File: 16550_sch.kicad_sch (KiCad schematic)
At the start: 1 part

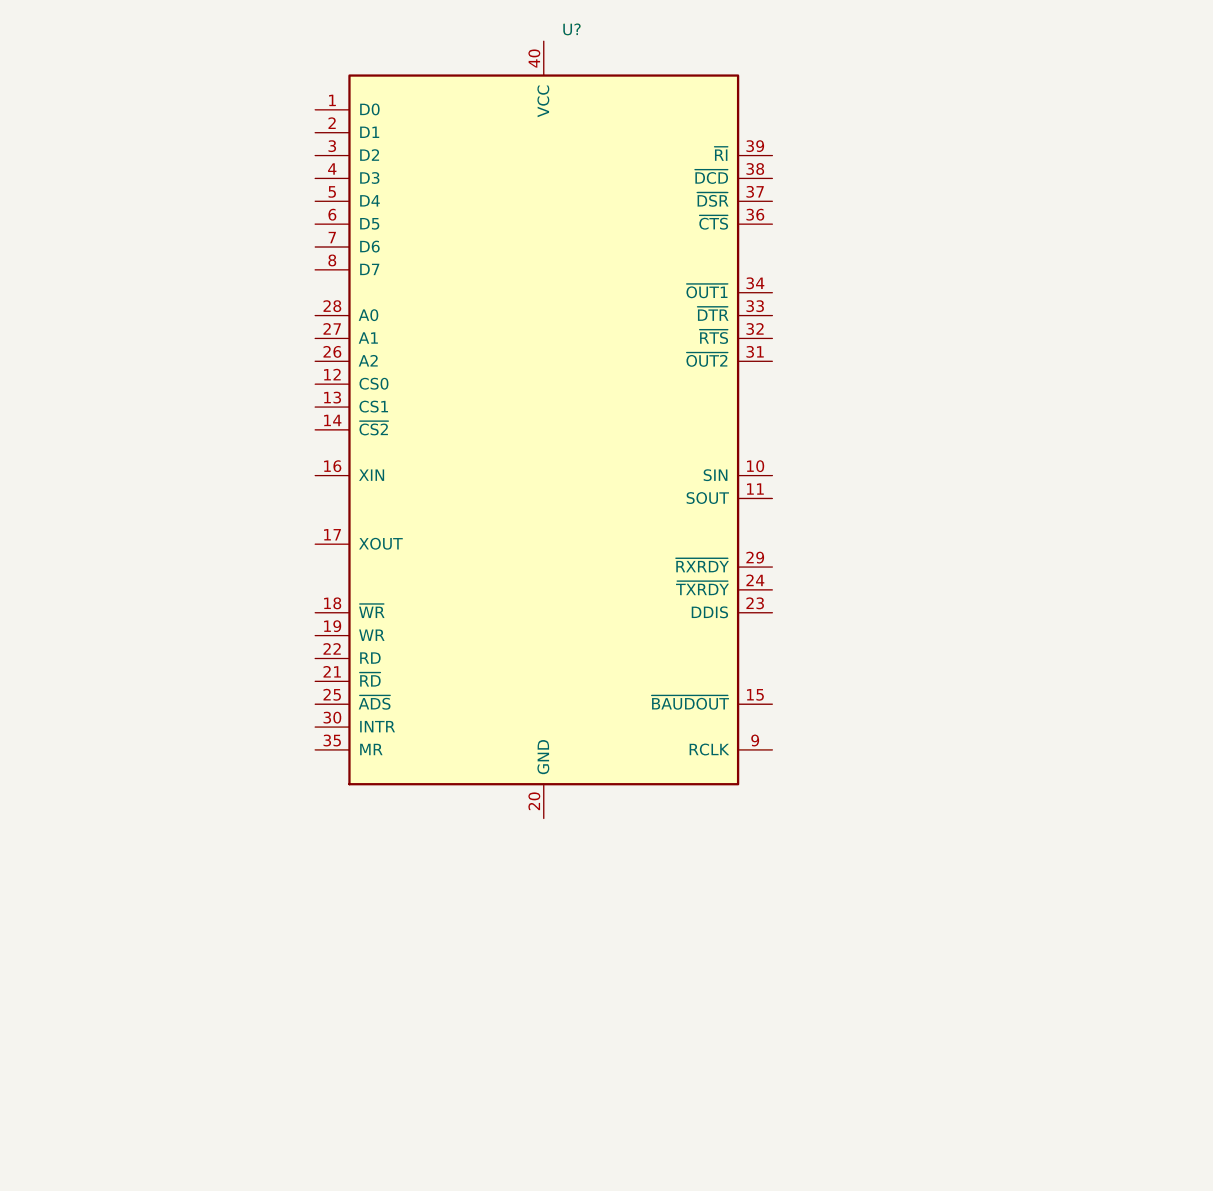
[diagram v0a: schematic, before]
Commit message: Wired the UART to the 8259A
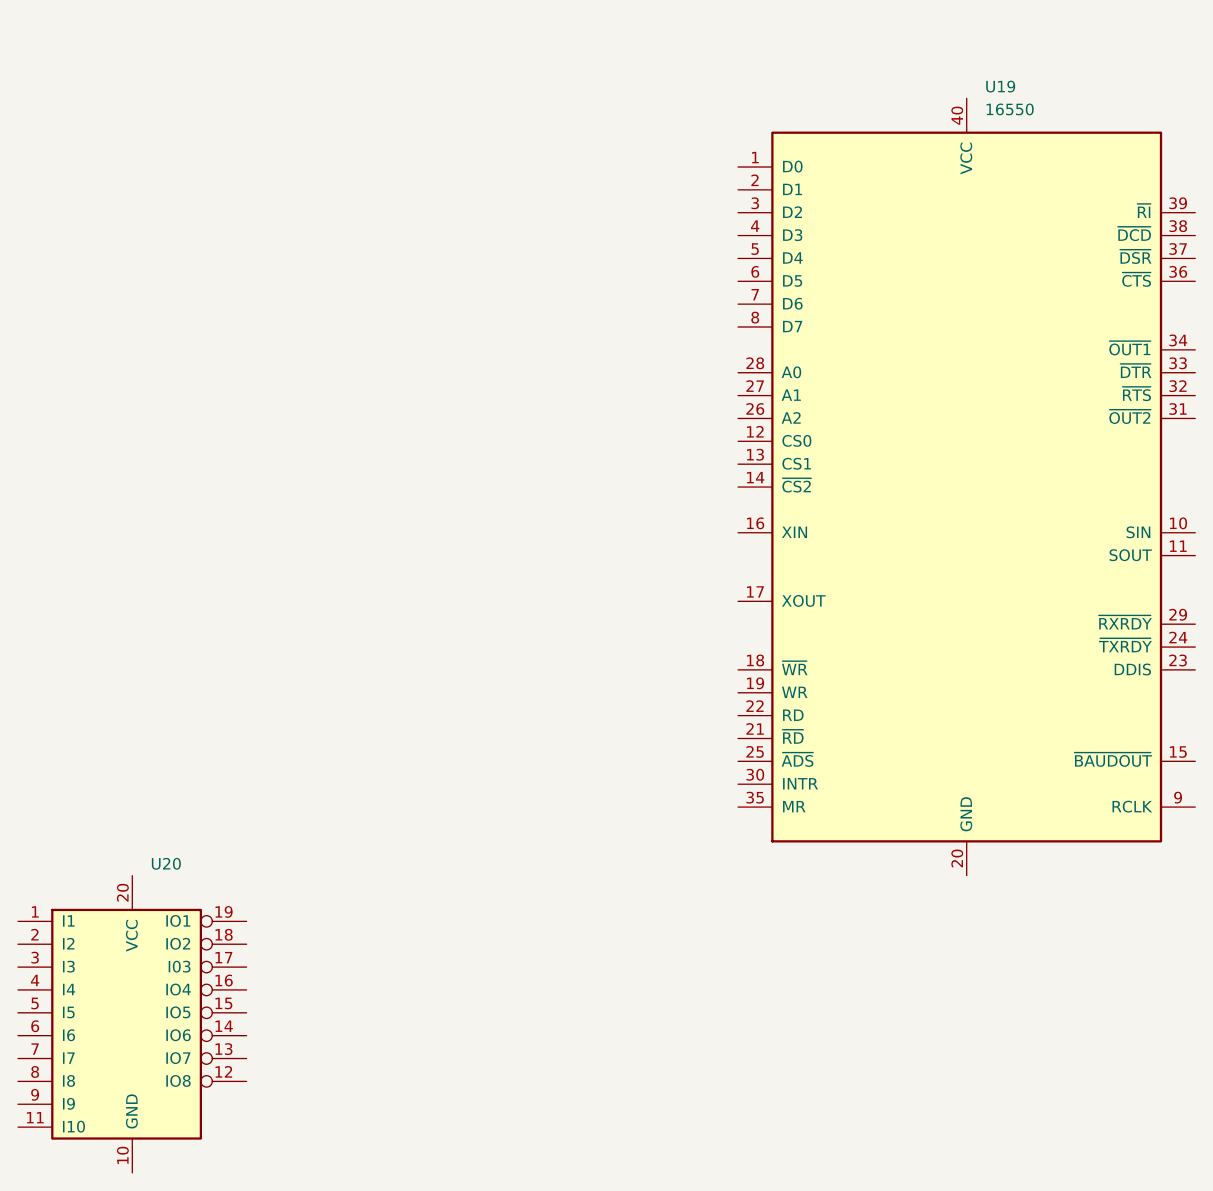
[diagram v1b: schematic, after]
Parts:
- added U20: (no value), symbol Logic_Programmable:PAL16L8
- U19: renamed from U?; value (none) -> 16550; footprint (none) -> Package_DIP:DIP-40_W15.24mm
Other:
- moved on the sheet: U19
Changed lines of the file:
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@@
 (kicad_sch (version 20211123) (generator eeschema)
   (paper "A4")
-  (symbol (lib_id "Interface_UART:16550") (at 116.84 69.85 0) (unit 1)
+  (symbol (lib_id "Interface_UART:16550") (at 163.83 76.2 0) (unit 1)
     (in_bom yes) (on_board yes) (fields_autoplaced)
-    (property "Reference" "U?" (id 0) (at 118.8594 25.4 0)
+    (property "Reference" "U19" (id 0) (at 165.8494 31.75 0)
       (effects (font (size 1.27 1.27)) (justify left))
     )
-    (property "Value" "" (id 1) (at 118.8594 27.94 0)
+    (property "Value" "16550" (id 1) (at 165.8494 34.29 0)
       (effects (font (size 1.27 1.27)) (justify left))
     )
-    (property "Footprint" "" (id 2) (at 116.84 69.85 0)
+    (property "Footprint" "Package_DIP:DIP-40_W15.24mm" (id 2) (at 163.83 76.2 0)
       (effects (font (size 1.27 1.27) italic) hide)
     )
-    (property "Datasheet" "http://www.ti.com/lit/ds/symlink/pc16550d.pdf" (id 3) (at 116.84 69.85 0)
+    (property "Datasheet" "http://www.ti.com/lit/ds/symlink/pc16550d.pdf" (id 3) (at 163.83 76.2 0)
       (effects (font (size 1.27 1.27)) hide)
     )
@@
     (pin "5")
     (pin "6")
+    (pin "7")
+    (pin "8")
+    (pin "9")
+  )
+  (symbol (lib_id "Logic_Programmable:PAL16L8") (at 71.12 137.16 0) (unit 1)
+    (in_bom yes) (on_board yes) (fields_autoplaced)
+    (property "Reference" "U20" (id 0) (at 73.1394 118.11 0)
+      (effects (font (size 1.27 1.27)) (justify left))
+    )
+    (property "Value" "" (id 1) (at 73.1394 120.65 0)
+      (effects (font (size 1.27 1.27)) (justify left))
+    )
+    (property "Footprint" "" (id 2) (at 71.12 137.16 0)
+      (effects (font (size 1.27 1.27)) hide)
+    )
+    (property "Datasheet" "" (id 3) (at 71.12 137.16 0)
+      (effects (font (size 1.27 1.27)) hide)
+    )
+    (pin "10")
+    (pin "20")
+    (pin "1")
+    (pin "11")
+    (pin "12")
+    (pin "13")
+    (pin "14")
+    (pin "15")
+    (pin "16")
+    (pin "17")
+    (pin "18")
+    (pin "19")
+    (pin "2")
+    (pin "3")
+    (pin "4")
+    (pin "5")
+    (pin "6")
